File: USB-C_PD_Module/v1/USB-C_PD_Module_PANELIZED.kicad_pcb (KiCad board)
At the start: 4 copper layers, 130.7 x 20.3 mm, 77 parts, among them J1 USB_C_Receptacle_USB2.0_16P, J2 Conn_01x10, J3 Conn_01x10, Q1 IRF7328TRPBF, U1 TPD4E02B04DQA, U2 TVS2200DRV, U3 TVS2200DRV, U4 CYPD3177-24LQ

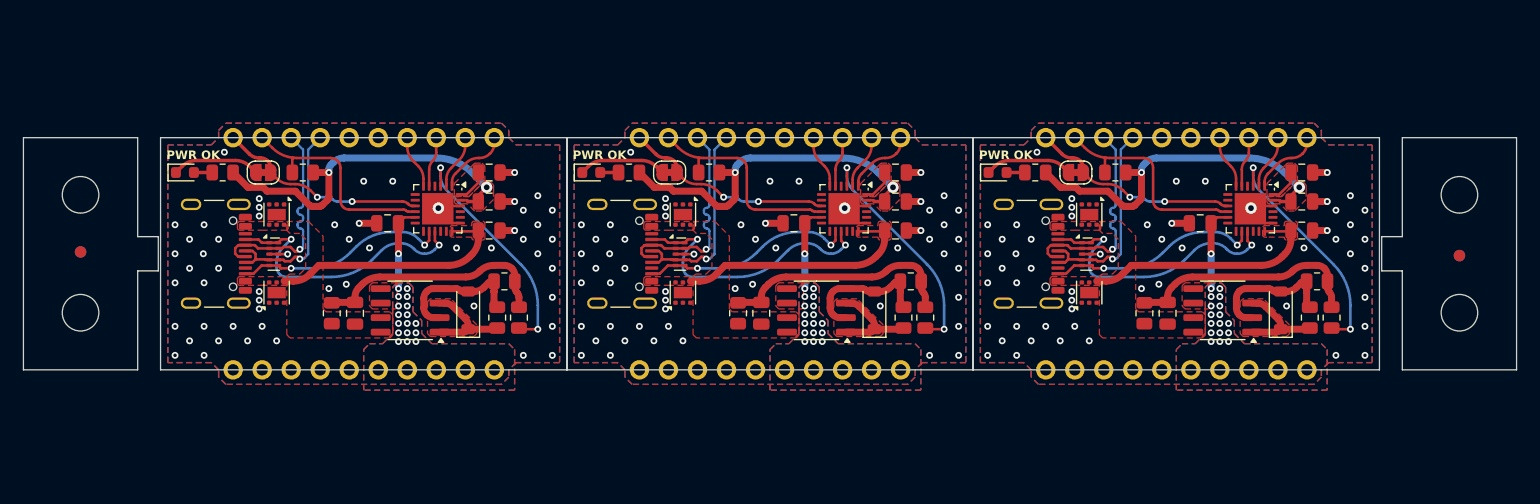
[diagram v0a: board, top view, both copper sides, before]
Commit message: withouut panel
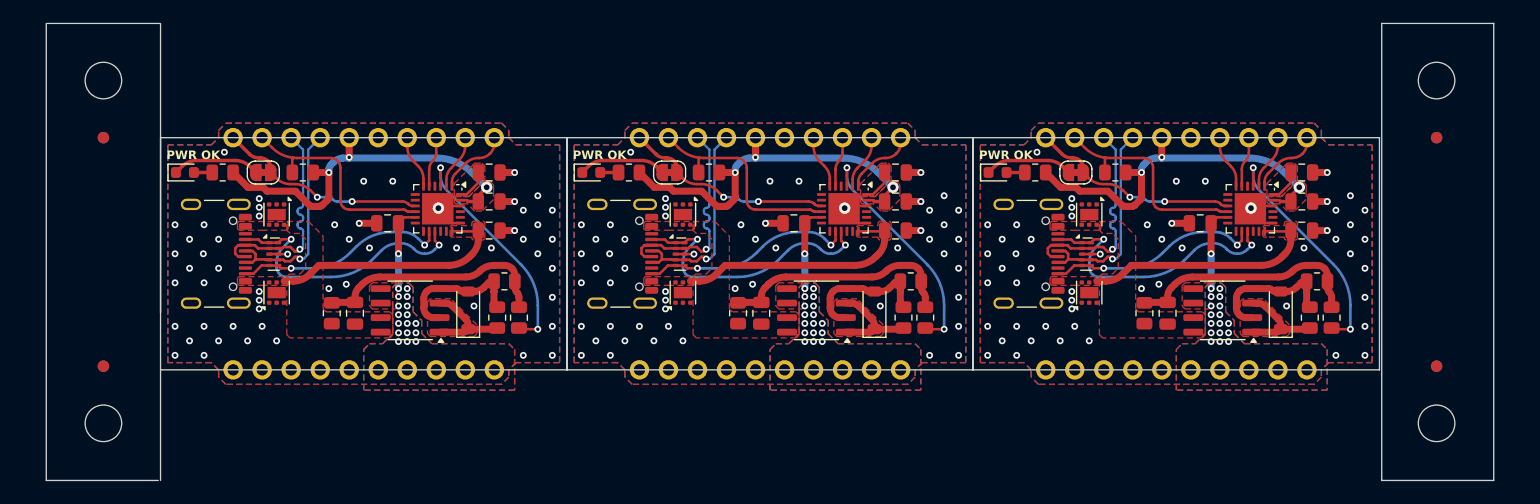
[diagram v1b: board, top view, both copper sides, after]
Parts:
- added KiKit_FID_B_2: Fiducial, Fiducial, B.Cu at (206.8, 20.0)
- added KiKit_FID_B_3: Fiducial, Fiducial, B.Cu at (90.2, 40.0)
- added KiKit_FID_T_2: Fiducial, Fiducial, F.Cu at (206.8, 20.0)
- added KiKit_FID_T_3: Fiducial, Fiducial, F.Cu at (90.2, 40.0)
- moved KiKit_FID_B_1 10.2 mm to (90.2, 20.0)
- moved KiKit_FID_T_1 10.2 mm to (90.2, 20.0)
- moved KiKit_TO_1 10.2 mm to (90.2, 15.0)
- moved KiKit_TO_2 10.2 mm to (206.8, 15.0)
- moved KiKit_FID_B_4 9.88 mm to (206.8, 40.0)
- moved KiKit_FID_T_4 9.88 mm to (206.8, 40.0)
- moved KiKit_TO_3 9.88 mm to (90.2, 45.0)
- moved KiKit_TO_4 9.88 mm to (206.8, 45.0)
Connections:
- J3 pad 5: Board_1-GND -> Board_1-+3V3
- J3 pad 5: Board_2-GND -> Board_2-+3V3
- J3 pad 5: Board_0-GND -> Board_0-+3V3
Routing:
- net Board_2-+3V3: track 32.1 -> 33.8 mm, vias 2 -> 3
- net Board_0-+3V3: track 32.1 -> 33.8 mm, vias 2 -> 3
- net Board_1-+3V3: track 32.1 -> 33.8 mm, vias 2 -> 3
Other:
- board size 130.7 x 20.3 mm -> 126.7 x 40 mm
- board text added: "VDDD"
